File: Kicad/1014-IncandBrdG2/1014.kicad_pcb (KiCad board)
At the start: 2 copper layers, 44.4 x 20.3 mm, 24 parts, among them P1 TST, P2 CONN_4, P3 CONN_4, P4 SPADE_187, P5 CONN_8, P6 CONN_2, P7 CONN_8, Q1 MOSFET_N, Q2 MOSFET_N, Q3 MOSFET_N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

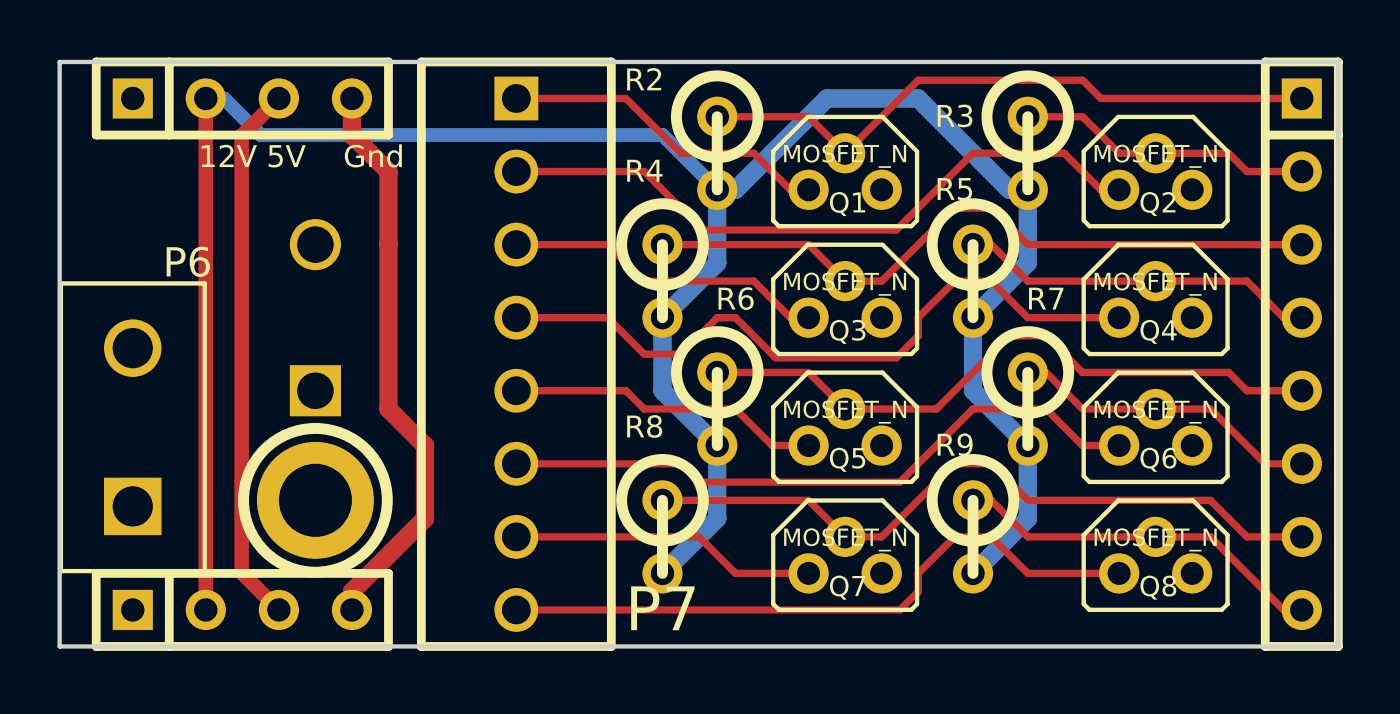
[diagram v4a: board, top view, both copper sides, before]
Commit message: 1014, Incandescent through-hole board:  Swapped to cheaper through-hole connector.  Added copper board revision. Panel-1014:  Added panellization of the board. Added MPF documentation on how to use OPP boards with MPF.
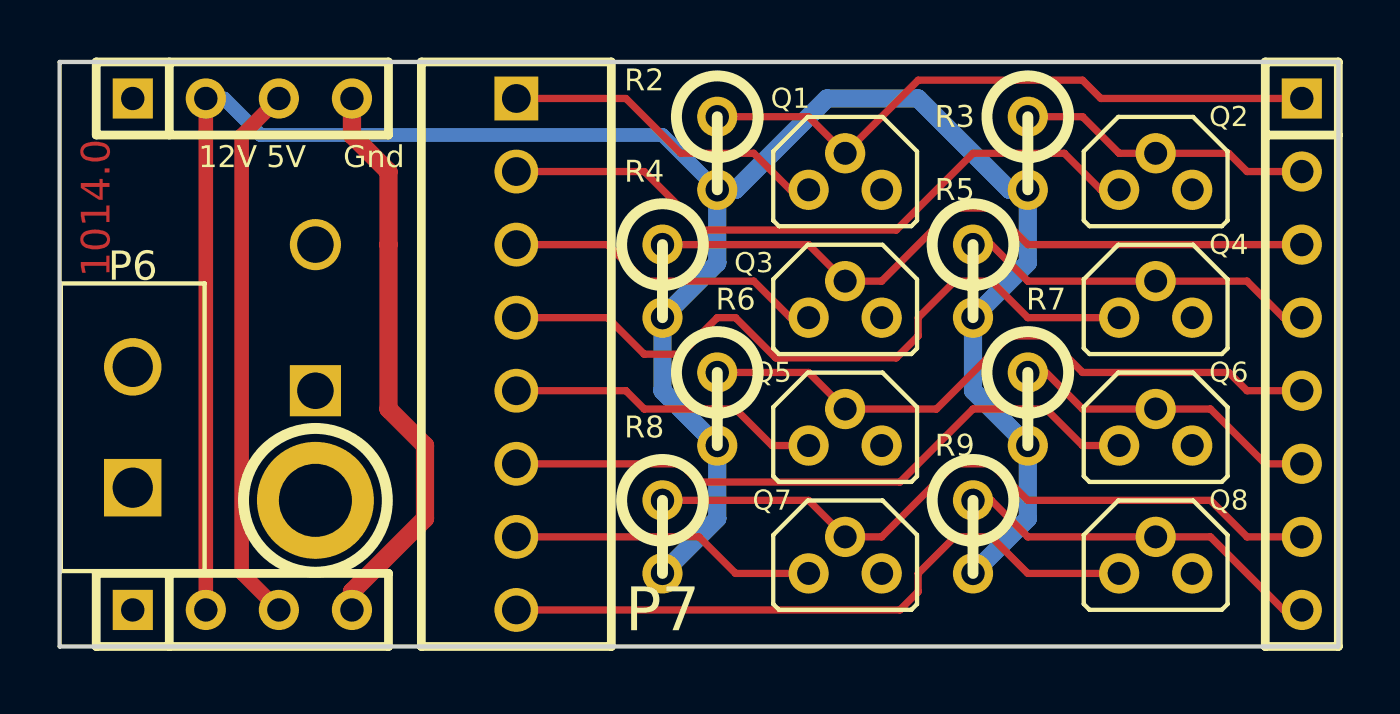
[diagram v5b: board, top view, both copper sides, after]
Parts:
- P6: footprint 00_th1x2x4.2mm_nopeg -> 00_th1x2x4.2mm_cheap
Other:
- board text added: "1014.0"
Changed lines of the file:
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@@
     (links 48)
     (no_connects 0)
-    (area 162.754734 140.529734 208.686401 161.696401)
+    (area 97.585953 66.869734 143.916401 88.036401)
     (thickness 1.6)
-    (drawings 7)
+    (drawings 8)
     (tracks 140)
     (zones 0)
@@
     (visible_elements 7FFFFFFF)
     (pcbplotparams
-      (layerselection 15761409)
+      (layerselection 284196865)
       (usegerberextensions true)
       (excludeedgelayer false)
@@
       (drillshape 0)
       (scaleselection 1)
-      (outputdirectory ""))
+      (outputdirectory Gerber/))
   )
   (net 0 "")
@@
     )
   )
-  (module 00_th1x2x4.2mm_nopeg (layer F.Cu)
-    (at 101.6 80.01)
-    (descr "Double rangee de contacts 2 x 8 pins")
-    (tags CONN)
-    (fp_text reference P6 (at 1.905 -5.715) (layer F.SilkS)
-      (effects (font (size 1.016 1.016) (thickness 0.2032)))
-    )
-    (fp_text value CONN_2 (at 0.127 0.127) (layer F.SilkS) hide
-      (effects (font (size 1.016 1.016) (thickness 0.2032)))
-    )
-    (fp_line (start -2.5 -5) (end 2.5 -5) (layer F.SilkS) (width 0.15))
-    (fp_line (start 2.5 -5) (end 2.5 5) (layer F.SilkS) (width 0.15))
-    (fp_line (start 2.5 5) (end -2.5 5) (layer F.SilkS) (width 0.15))
-    (fp_line (start -2.5 5) (end -2.5 -5) (layer F.SilkS) (width 0.15))
-    (pad 1 thru_hole rect (at 0 2.75082) (size 1.99898 1.99898) (drill 1.39954)
-      (layers *.Cu *.Mask F.SilkS)
-      (net 3 +VLED)
-    )
-    (pad 2 thru_hole circle (at 0 -2.75082) (size 1.99898 1.99898) (drill 1.39954)
-      (layers *.Cu *.Mask F.SilkS)
-      (net 3 +VLED)
-    )
-    (model pin_array/pins_array_8x2.wrl
-      (at (xyz 0 0 0))
-      (scale (xyz 1 1 1))
-      (rotate (xyz 0 0 0))
-    )
-  )
   (module 00_th1x2x200 (layer F.Cu)
     (at 107.95 76.2 90)
@@
   (module 00_to92_sgd (layer F.Cu)
     (at 126.365 75.565 180)
-    (fp_text reference Q3 (at -0.1 -1.1 180) (layer F.SilkS)
+    (fp_text reference Q3 (at 3.175 1.27 180) (layer F.SilkS)
       (effects (font (size 0.7 0.7) (thickness 0.15)))
     )
-    (fp_text value MOSFET_N (at 0 0.6 180) (layer F.SilkS)
+    (fp_text value MOSFET_N (at 0 0.6 180) (layer F.SilkS) hide
       (effects (font (size 0.6 0.6) (thickness 0.15)))
     )
@@
   (module 00_to92_sgd (layer F.Cu)
     (at 137.16 75.565 180)
-    (fp_text reference Q4 (at -0.1 -1.1 180) (layer F.SilkS)
+    (fp_text reference Q4 (at -2.54 1.905 180) (layer F.SilkS)
       (effects (font (size 0.7 0.7) (thickness 0.15)))
     )
-    (fp_text value MOSFET_N (at 0 0.6 180) (layer F.SilkS)
+    (fp_text value MOSFET_N (at 0 0.6 180) (layer F.SilkS) hide
       (effects (font (size 0.6 0.6) (thickness 0.15)))
     )
@@
   (module 00_to92_sgd (layer F.Cu)
     (at 137.16 71.12 180)
-    (fp_text reference Q2 (at -0.1 -1.1 180) (layer F.SilkS)
+    (fp_text reference Q2 (at -2.54 1.905 180) (layer F.SilkS)
       (effects (font (size 0.7 0.7) (thickness 0.15)))
     )
-    (fp_text value MOSFET_N (at 0 0.6 180) (layer F.SilkS)
+    (fp_text value MOSFET_N (at 0 0.6 180) (layer F.SilkS) hide
       (effects (font (size 0.6 0.6) (thickness 0.15)))
     )
@@
   (module 00_to92_sgd (layer F.Cu)
     (at 126.365 80.01 180)
-    (fp_text reference Q5 (at -0.1 -1.1 180) (layer F.SilkS)
+    (fp_text reference Q5 (at 2.54 1.905 180) (layer F.SilkS)
       (effects (font (size 0.7 0.7) (thickness 0.15)))
     )
-    (fp_text value MOSFET_N (at 0 0.6 180) (layer F.SilkS)
+    (fp_text value MOSFET_N (at 0 0.6 180) (layer F.SilkS) hide
       (effects (font (size 0.6 0.6) (thickness 0.15)))
     )
@@
   (module 00_to92_sgd (layer F.Cu)
     (at 137.16 80.01 180)
-    (fp_text reference Q6 (at -0.1 -1.1 180) (layer F.SilkS)
+    (fp_text reference Q6 (at -2.54 1.905 180) (layer F.SilkS)
       (effects (font (size 0.7 0.7) (thickness 0.15)))
     )
-    (fp_text value MOSFET_N (at 0 0.6 180) (layer F.SilkS)
+    (fp_text value MOSFET_N (at 0 0.6 180) (layer F.SilkS) hide
       (effects (font (size 0.6 0.6) (thickness 0.15)))
     )
@@
   (module 00_to92_sgd (layer F.Cu)
     (at 126.365 84.455 180)
-    (fp_text reference Q7 (at -0.1 -1.1 180) (layer F.SilkS)
+    (fp_text reference Q7 (at 2.54 1.905 180) (layer F.SilkS)
       (effects (font (size 0.7 0.7) (thickness 0.15)))
     )
-    (fp_text value MOSFET_N (at 0 0.6 180) (layer F.SilkS)
+    (fp_text value MOSFET_N (at 0 0.6 180) (layer F.SilkS) hide
       (effects (font (size 0.6 0.6) (thickness 0.15)))
     )
@@
   (module 00_to92_sgd (layer F.Cu)
     (at 137.16 84.455 180)
-    (fp_text reference Q8 (at -0.1 -1.1 180) (layer F.SilkS)
+    (fp_text reference Q8 (at -2.54 1.905 180) (layer F.SilkS)
       (effects (font (size 0.7 0.7) (thickness 0.15)))
     )
-    (fp_text value MOSFET_N (at 0 0.6 180) (layer F.SilkS)
+    (fp_text value MOSFET_N (at 0 0.6 180) (layer F.SilkS) hide
       (effects (font (size 0.6 0.6) (thickness 0.15)))
     )
@@
   (module 00_to92_sgd (layer F.Cu)
     (at 126.365 71.12 180)
-    (fp_text reference Q1 (at -0.1 -1.1 180) (layer F.SilkS)
+    (fp_text reference Q1 (at 1.905 2.54 180) (layer F.SilkS)
       (effects (font (size 0.7 0.7) (thickness 0.15)))
     )
-    (fp_text value MOSFET_N (at 0 0.6 180) (layer F.SilkS)
+    (fp_text value MOSFET_N (at 0 0.6 180) (layer F.SilkS) hide
       (effects (font (size 0.6 0.6) (thickness 0.15)))
     )
@@
       (xy -1.6764 -1.524) (xy -1.7145 -1.50114) (xy -1.7272 -1.47066) (xy -1.7272 -1.47066)) (layer B.SilkS) (width 0.00254))
   )
+  (module 00_th1x2x4.2mm_cheap (layer F.Cu)
+    (at 101.6 80.01)
+    (descr "Double rangee de contacts 2 x 8 pins")
+    (tags CONN)
+    (fp_text reference P6 (at 0 -5.6007) (layer F.SilkS)
+      (effects (font (size 1.016 1.016) (thickness 0.2032)))
+    )
+    (fp_text value CONN_2 (at 0.127 0.127) (layer F.SilkS) hide
+      (effects (font (size 1.016 1.016) (thickness 0.2032)))
+    )
+    (fp_line (start -2.5 -5) (end 2.5 -5) (layer F.SilkS) (width 0.15))
+    (fp_line (start 2.5 -5) (end 2.5 5) (layer F.SilkS) (width 0.15))
+    (fp_line (start 2.5 5) (end -2.5 5) (layer F.SilkS) (width 0.15))
+    (fp_line (start -2.5 5) (end -2.5 -5) (layer F.SilkS) (width 0.15))
+    (pad 1 thru_hole rect (at 0 2.1) (size 1.99898 1.99898) (drill 1.39954)
+      (layers *.Cu *.Mask F.SilkS)
+      (net 3 +VLED)
+    )
+    (pad 2 thru_hole circle (at 0 -2.1) (size 1.99898 1.99898) (drill 1.39954)
+      (layers *.Cu *.Mask F.SilkS)
+      (net 3 +VLED)
+    )
+    (model pin_array/pins_array_8x2.wrl
+      (at (xyz 0 0 0))
+      (scale (xyz 1 1 1))
+      (rotate (xyz 0 0 0))
+    )
+  )
+  (gr_text 1014.0 (at 100.33 72.39 90) (layer F.Cu)
+    (effects (font (size 1 1) (thickness 0.25)))
+  )
   (gr_text Gnd (at 109.982 70.612) (layer F.SilkS)

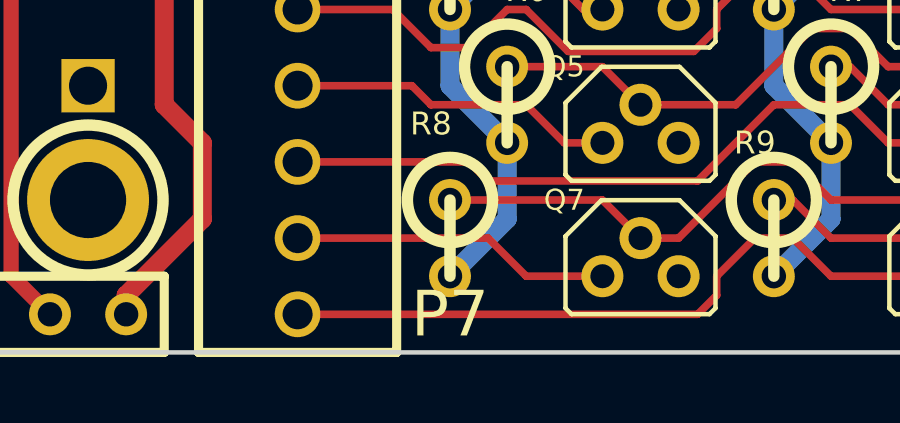
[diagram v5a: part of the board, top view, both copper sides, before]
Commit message: Kicad updates: Added IncandWing (1014.zip), PwrFilter (1018.zip), updated Sol Panel (Panel-1013.zip), Incand Panel (Panel-1014.zip), and Pwr Filter Panel (Panel-1018.zip).  Panels had a different drill origin than PCB origin.
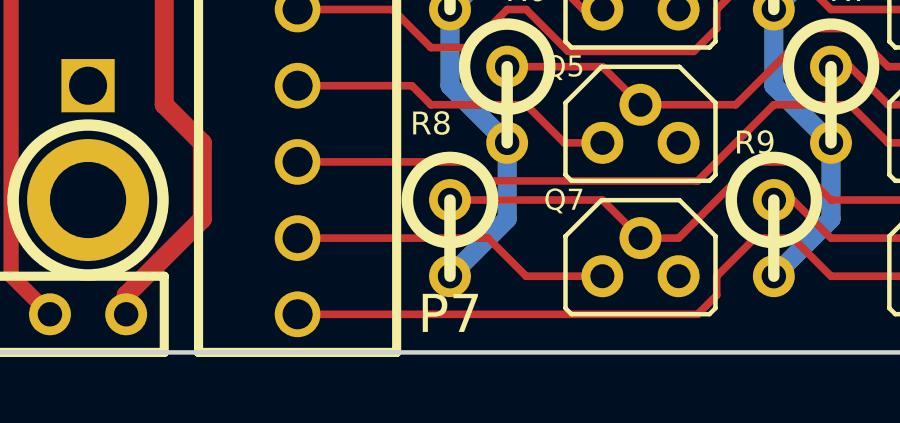
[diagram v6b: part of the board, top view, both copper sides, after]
